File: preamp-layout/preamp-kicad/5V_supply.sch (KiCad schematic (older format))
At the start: 20 parts, among them J10 Conn_01x02_Male, J11 Conn_01x02_Male, J12 Conn_01x02_Male, J9 Screw_Terminal_01x03, T2 Transformer_1P_2S, U3 L7805

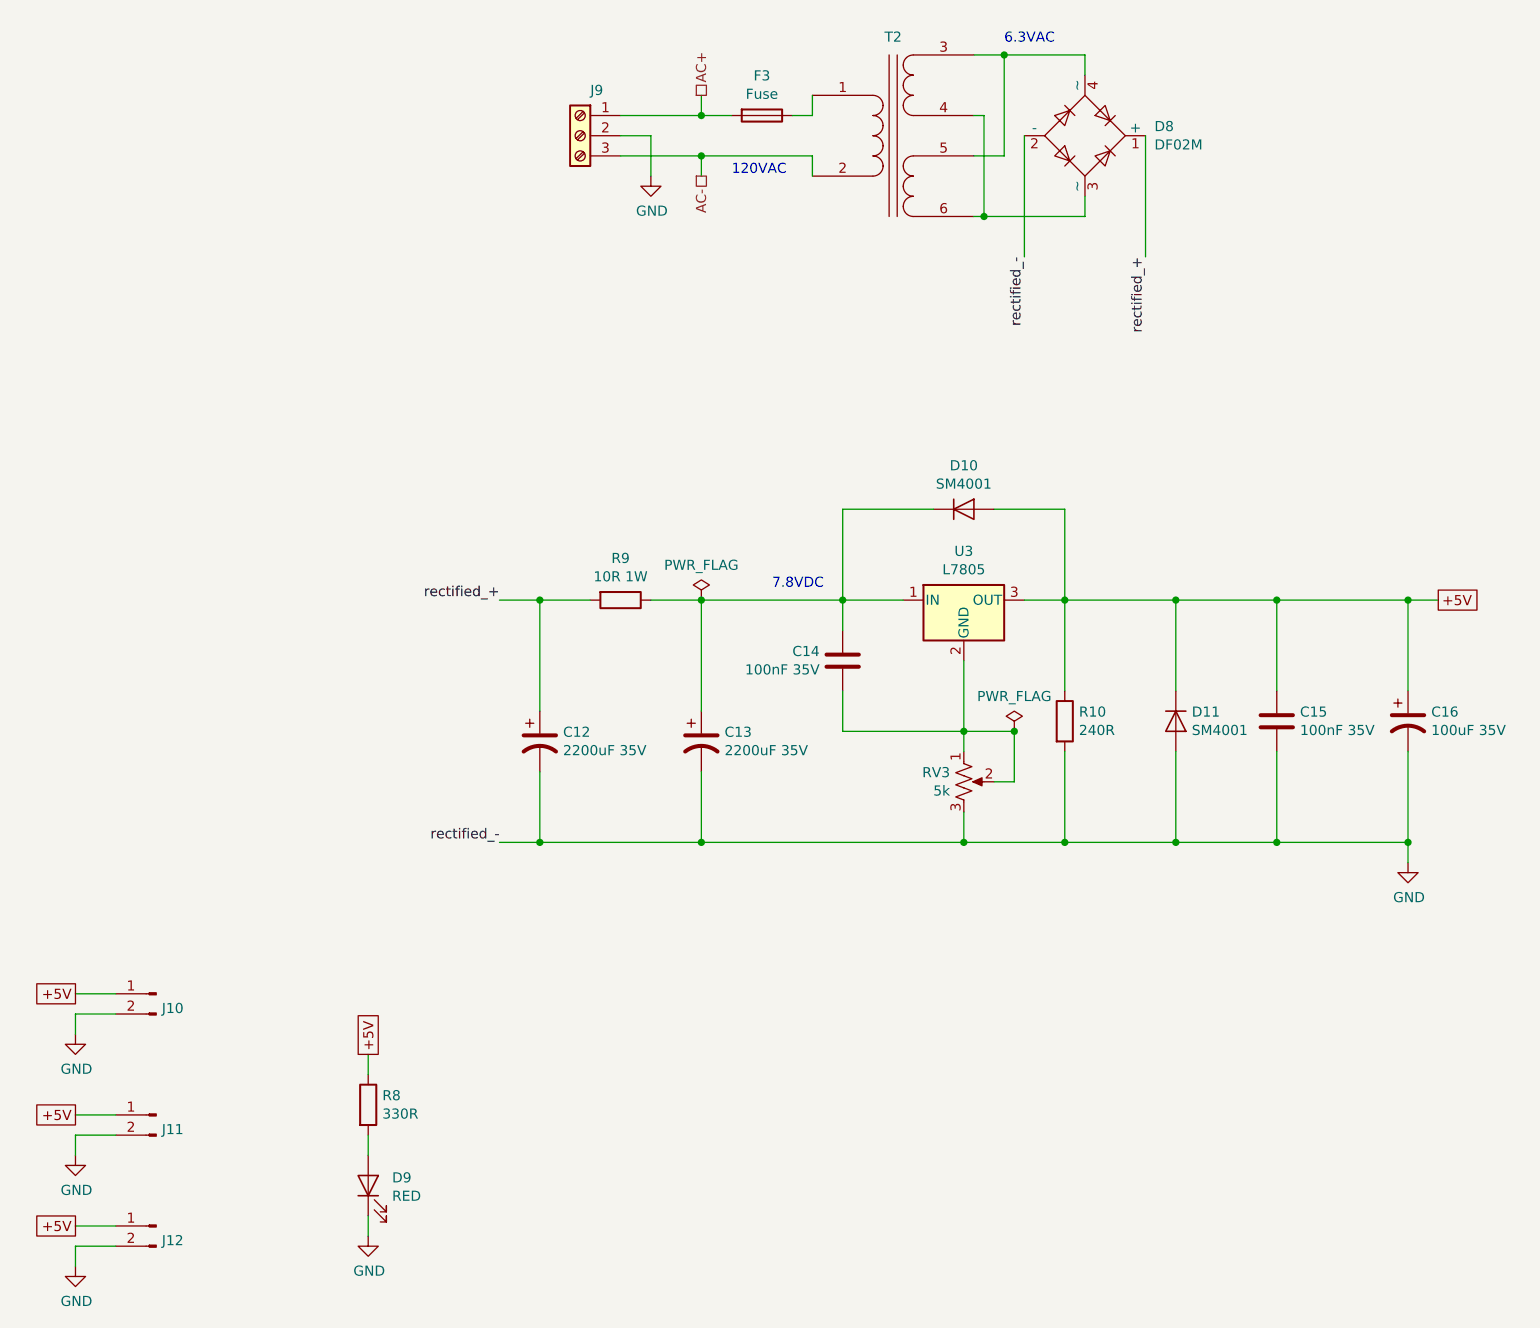
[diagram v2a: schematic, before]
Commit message: BOM Update
parts added to BOM, connector cleanup. Stopping point before renumbering refdes in a more intelligent way.
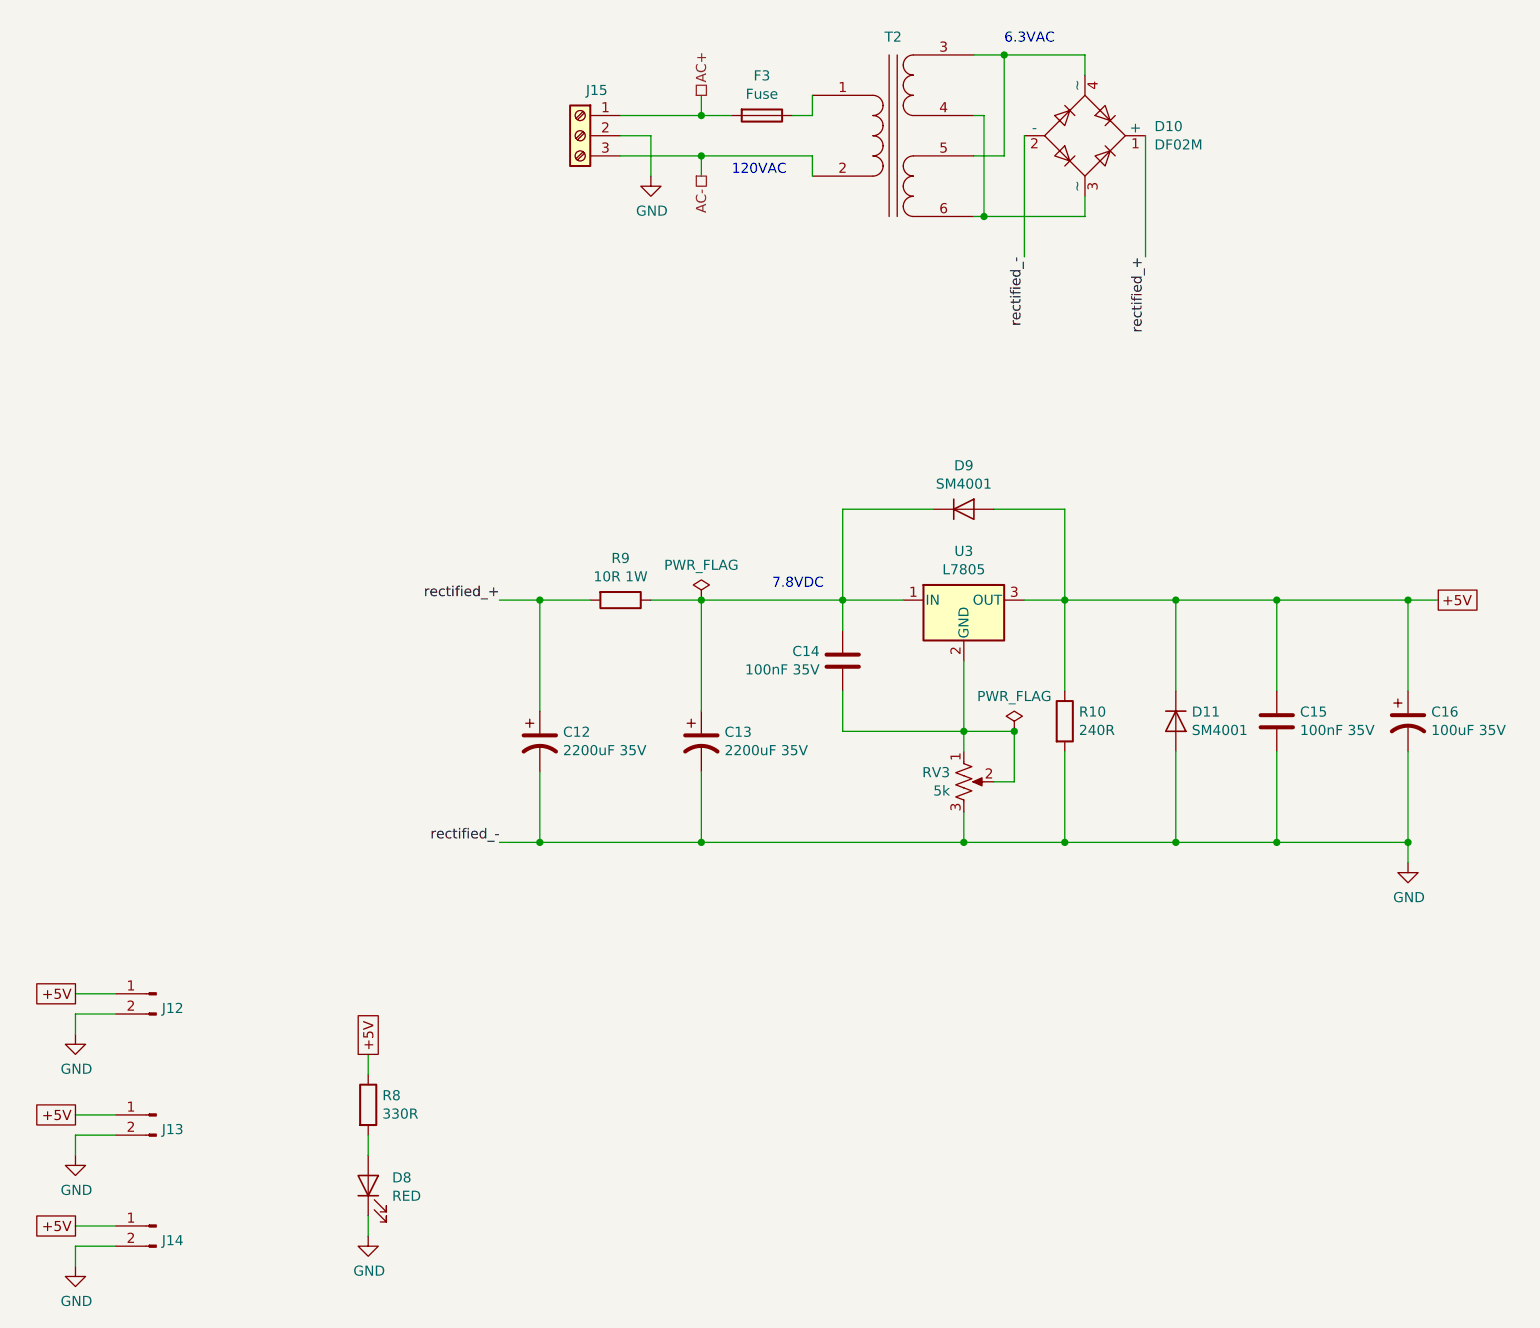
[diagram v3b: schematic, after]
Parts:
- renumbered D8 to D10, D9 to D8, D10 to D9, J10 to J12, J11 to J13, J12 to J14, J9 to J15
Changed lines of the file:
@@
 AR Path="/5FCCFC72" Ref="D?"  Part="1"
 AR Path="/5E27B612/5FCCFC72" Ref="D?"  Part="1"
-AR Path="/5E5EF2D4/5FCCFC72" Ref="D10"  Part="1"
-F 0 "D10" H 5950 3566 50  0000 C CNN
+AR Path="/5E5EF2D4/5FCCFC72" Ref="D9"  Part="1"
+F 0 "D9" H 5950 3566 50  0000 C CNN
 F 1 "SM4001" H 5950 3475 50  0000 C CNN
 F 2 "" H 5950 3350 50  0001 C CNN
@@
 AR Path="/5E2D8DA2/5FCCFD41" Ref="D?"  Part="1"
 AR Path="/5E27B612/5FCCFD41" Ref="D?"  Part="1"
-AR Path="/5E5EF2D4/5FCCFD41" Ref="D9"  Part="1"
-F 0 "D9" V 3039 6582 50  0000 R CNN
+AR Path="/5E5EF2D4/5FCCFD41" Ref="D8"  Part="1"
+F 0 "D8" V 3039 6582 50  0000 R CNN
 F 1 "RED" V 2948 6582 50  0000 R CNN
 F 2 "LED_SMD:LED_1206_3216Metric_Pad1.42x1.75mm_HandSolder" H 3000 6700 50  0001 C CNN
@@
 rectified_+
 $Comp
-L Connector:Conn_01x02_Male J10
+L Connector:Conn_01x02_Male J12
 U 1 1 5FD21456
 P 1950 5750
-F 0 "J10" H 1922 5678 50  0000 R CNN
+F 0 "J12" H 1922 5678 50  0000 R CNN
 F 1 "Conn_01x02_Male" H 1922 5633 50  0001 R CNN
 F 2 "Connector_JST:JST_EH_B2B-EH-A_1x02_P2.50mm_Vertical" H 1950 5750 50  0001 C CNN
@@
 	1750 5750 1550 5750
 $Comp
-L Connector:Conn_01x02_Male J11
+L Connector:Conn_01x02_Male J13
 U 1 1 5FD3E35C
 P 1950 6350
-F 0 "J11" H 1922 6278 50  0000 R CNN
+F 0 "J13" H 1922 6278 50  0000 R CNN
 F 1 "Conn_01x02_Male" H 1922 6233 50  0001 R CNN
 F 2 "Connector_JST:JST_EH_B2B-EH-A_1x02_P2.50mm_Vertical" H 1950 6350 50  0001 C CNN
@@
 	1750 6350 1550 6350
 $Comp
-L Connector:Conn_01x02_Male J12
+L Connector:Conn_01x02_Male J14
 U 1 1 5FD41D04
 P 1950 6900
-F 0 "J12" H 1922 6828 50  0000 R CNN
+F 0 "J14" H 1922 6828 50  0000 R CNN
 F 1 "Conn_01x02_Male" H 1922 6783 50  0001 R CNN
 F 2 "Connector_JST:JST_EH_B2B-EH-A_1x02_P2.50mm_Vertical" H 1950 6900 50  0001 C CNN
@@
 P 6550 1500
 AR Path="/5E27B612/5FD91DA0" Ref="D?"  Part="1"
-AR Path="/5E5EF2D4/5FD91DA0" Ref="D8"  Part="1"
-F 0 "D8" H 6894 1546 50  0000 L CNN
+AR Path="/5E5EF2D4/5FD91DA0" Ref="D10"  Part="1"
+F 0 "D10" H 6894 1546 50  0000 L CNN
 F 1 "DF02M" H 6894 1455 50  0000 L CNN
 F 2 "Diode_THT:Diode_Bridge_DIP-4_W7.62mm_P5.08mm" H 6700 1625 50  0001 L CNN
@@
 P 1550 5950
 AR Path="/5E26F6FE/64A240A6" Ref="#PWR?"  Part="1"
-AR Path="/5E5EF2D4/64A240A6" Ref="#PWR010"  Part="1"
-F 0 "#PWR010" H 1550 5700 50  0001 C CNN
+AR Path="/5E5EF2D4/64A240A6" Ref="#PWR013"  Part="1"
+F 0 "#PWR013" H 1550 5700 50  0001 C CNN
 F 1 "GND" H 1555 5777 50  0000 C CNN
 F 2 "" H 1550 5950 50  0001 C CNN
@@
 P 1550 6550
 AR Path="/5E26F6FE/64A2D7ED" Ref="#PWR?"  Part="1"
-AR Path="/5E5EF2D4/64A2D7ED" Ref="#PWR011"  Part="1"
-F 0 "#PWR011" H 1550 6300 50  0001 C CNN
+AR Path="/5E5EF2D4/64A2D7ED" Ref="#PWR014"  Part="1"
+F 0 "#PWR014" H 1550 6300 50  0001 C CNN
 F 1 "GND" H 1555 6377 50  0000 C CNN
 F 2 "" H 1550 6550 50  0001 C CNN
@@
 P 1550 7100
 AR Path="/5E26F6FE/64A2F0C8" Ref="#PWR?"  Part="1"
-AR Path="/5E5EF2D4/64A2F0C8" Ref="#PWR012"  Part="1"
-F 0 "#PWR012" H 1550 6850 50  0001 C CNN
+AR Path="/5E5EF2D4/64A2F0C8" Ref="#PWR015"  Part="1"
+F 0 "#PWR015" H 1550 6850 50  0001 C CNN
 F 1 "GND" H 1555 6927 50  0000 C CNN
 F 2 "" H 1550 7100 50  0001 C CNN
@@
 P 3000 6950
 AR Path="/5E26F6FE/64A323D4" Ref="#PWR?"  Part="1"
-AR Path="/5E5EF2D4/64A323D4" Ref="#PWR013"  Part="1"
-F 0 "#PWR013" H 3000 6700 50  0001 C CNN
+AR Path="/5E5EF2D4/64A323D4" Ref="#PWR016"  Part="1"
+F 0 "#PWR016" H 3000 6700 50  0001 C CNN
 F 1 "GND" H 3005 6777 50  0000 C CNN
 F 2 "" H 3000 6950 50  0001 C CNN
@@
 P 8150 5100
 AR Path="/5E26F6FE/64A33F46" Ref="#PWR?"  Part="1"
-AR Path="/5E5EF2D4/64A33F46" Ref="#PWR014"  Part="1"
-F 0 "#PWR014" H 8150 4850 50  0001 C CNN
+AR Path="/5E5EF2D4/64A33F46" Ref="#PWR018"  Part="1"
+F 0 "#PWR018" H 8150 4850 50  0001 C CNN
 F 1 "GND" H 8155 4927 50  0000 C CNN
 F 2 "" H 8150 5100 50  0001 C CNN
@@
 P 4050 1500
 AR Path="/5E26F6FE/5E8DD1BE" Ref="J?"  Part="1"
-AR Path="/5E5EF2D4/5E8DD1BE" Ref="J9"  Part="1"
-F 0 "J9" H 3968 1725 50  0000 C CNN
+AR Path="/5E5EF2D4/5E8DD1BE" Ref="J15"  Part="1"
+F 0 "J15" H 3968 1725 50  0000 C CNN
 F 1 "Screw_Terminal_01x03" H 3968 1266 50  0001 C CNN
 F 2 "TerminalBlock_Phoenix:TerminalBlock_Phoenix_MKDS-3-3-5.08_1x03_P5.08mm_Horizontal" H 4050 1500 50  0001 C CNN
@@
 P 4400 1700
 AR Path="/5E26F6FE/5E8EF23A" Ref="#PWR?"  Part="1"
-AR Path="/5E5EF2D4/5E8EF23A" Ref="#PWR0113"  Part="1"
-F 0 "#PWR0113" H 4400 1450 50  0001 C CNN
+AR Path="/5E5EF2D4/5E8EF23A" Ref="#PWR017"  Part="1"
+F 0 "#PWR017" H 4400 1450 50  0001 C CNN
 F 1 "GND" H 4405 1527 50  0000 C CNN
 F 2 "" H 4400 1700 50  0001 C CNN

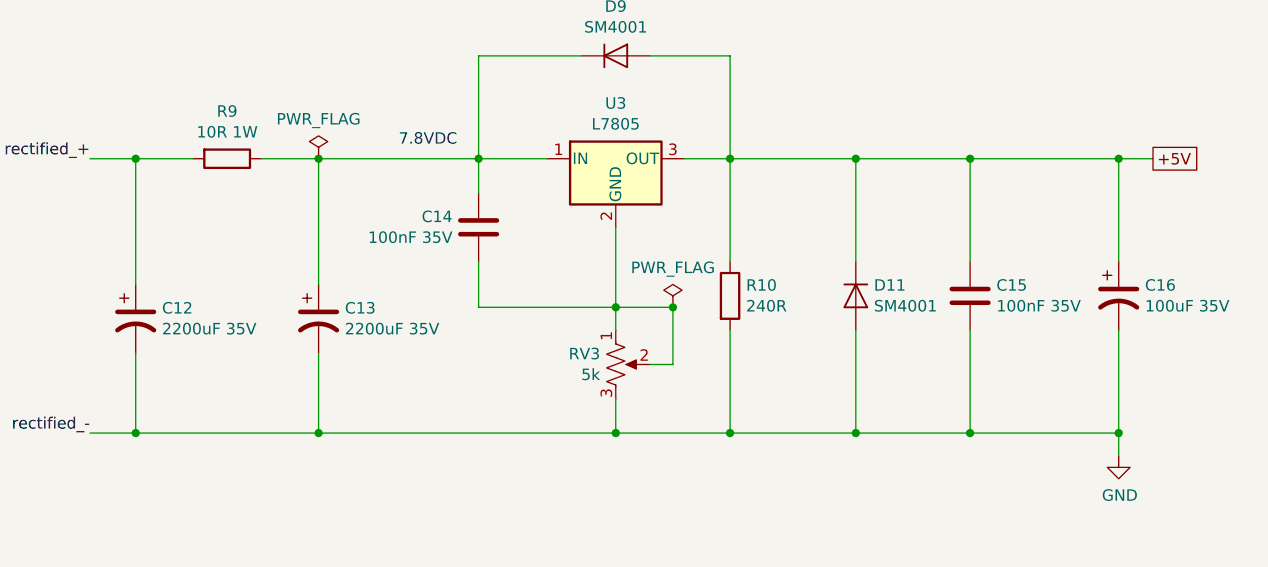
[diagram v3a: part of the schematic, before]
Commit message: Schematic Redesignation
Regenerated RefDes for all parts, updated BOM accordingly and perfomred check on values, RefDes present from schematic to BOM. Value changes, BOM filled in as a result.
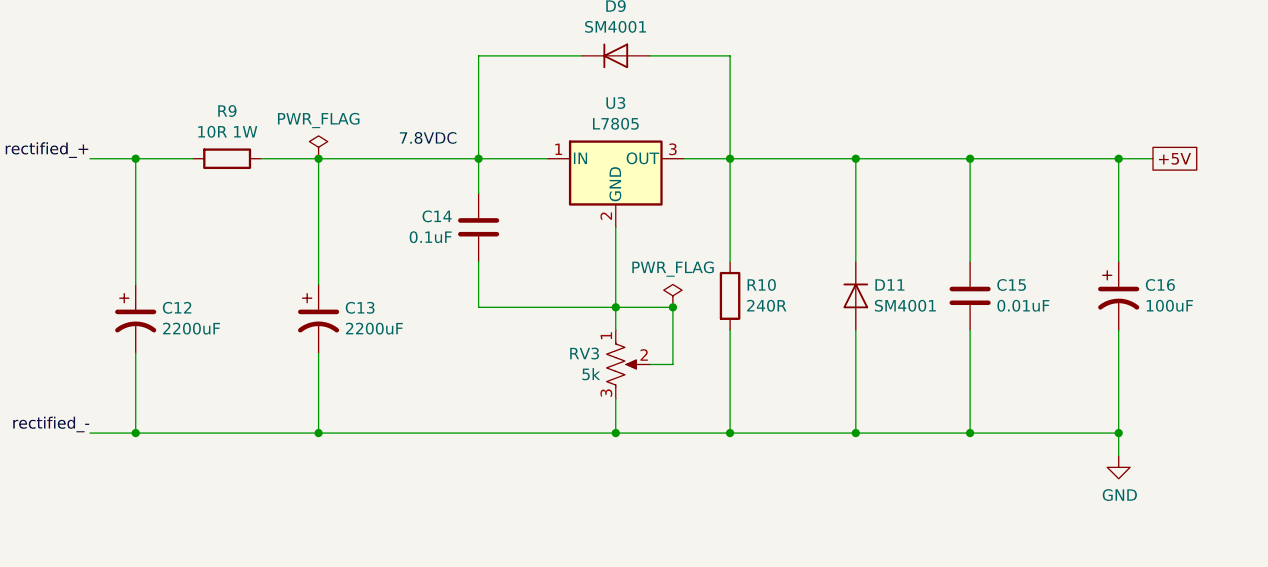
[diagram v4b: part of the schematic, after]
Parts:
- C12, C13: value 2200uF 35V -> 2200uF
- C14: value 100nF 35V -> 0.1uF
- C15: value 100nF 35V -> 0.01uF
- C16: value 100uF 35V -> 100uF
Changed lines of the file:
@@
 AR Path="/5E5EF2D4/5FCCFC4E" Ref="C15"  Part="1"
 F 0 "C15" H 7615 4446 50  0000 L CNN
-F 1 "100nF 35V" H 7615 4355 50  0000 L CNN
+F 1 "0.01uF" H 7615 4355 50  0000 L CNN
 F 2 "" H 7538 4250 50  0001 C CNN
 F 3 "~" H 7500 4400 50  0001 C CNN
@@
 AR Path="/5E5EF2D4/5FCCFCB8" Ref="C14"  Part="1"
 F 0 "C14" H 5236 4146 50  0000 R CNN
-F 1 "100nF 35V" H 5236 4055 50  0000 R CNN
+F 1 "0.1uF" H 5236 4055 50  0000 R CNN
 F 2 "" H 5388 3950 50  0001 C CNN
 F 3 "~" H 5350 4100 50  0001 C CNN
@@
 AR Path="/5E5EF2D4/5FCCFCBE" Ref="C12"  Part="1"
 F 0 "C12" H 3965 4546 50  0000 L CNN
-F 1 "2200uF 35V" H 3965 4455 50  0000 L CNN
+F 1 "2200uF" H 3965 4455 50  0000 L CNN
 F 2 "" H 3850 4500 50  0001 C CNN
 F 3 "~" H 3850 4500 50  0001 C CNN
@@
 AR Path="/5E5EF2D4/5FCCFCC4" Ref="C13"  Part="1"
 F 0 "C13" H 4765 4546 50  0000 L CNN
-F 1 "2200uF 35V" H 4765 4455 50  0000 L CNN
+F 1 "2200uF" H 4765 4455 50  0000 L CNN
 F 2 "" H 4650 4500 50  0001 C CNN
 F 3 "~" H 4650 4500 50  0001 C CNN
@@
 AR Path="/5E5EF2D4/5FCCFD14" Ref="C16"  Part="1"
 F 0 "C16" H 8265 4446 50  0000 L CNN
-F 1 "100uF 35V" H 8265 4355 50  0000 L CNN
+F 1 "100uF" H 8265 4355 50  0000 L CNN
 F 2 "" H 8150 4400 50  0001 C CNN
 F 3 "~" H 8150 4400 50  0001 C CNN
